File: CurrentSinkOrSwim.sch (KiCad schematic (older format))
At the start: 3 parts, among them P101 CONN_01X02, P102 CONN_01X03, P103 CONN_01X02

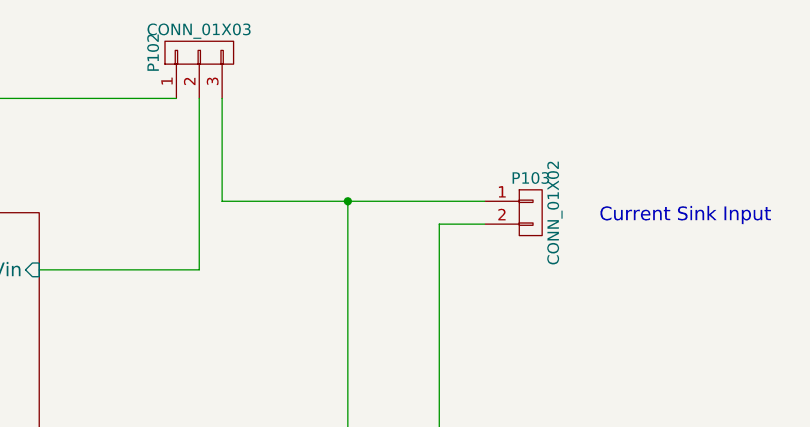
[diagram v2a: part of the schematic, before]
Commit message: added test points to  schematic and pcb
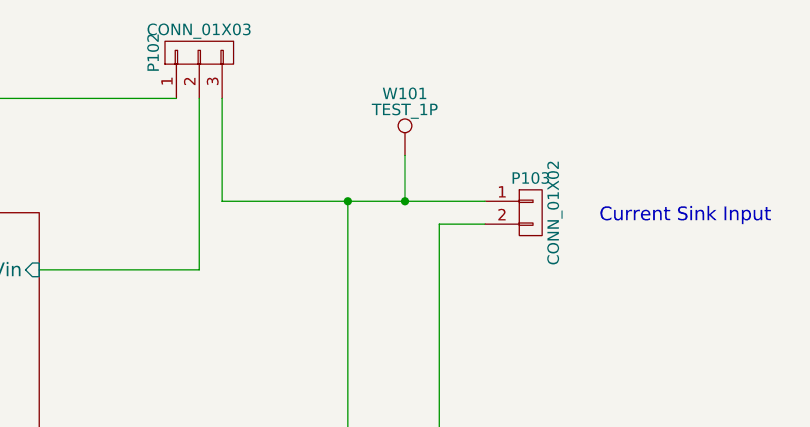
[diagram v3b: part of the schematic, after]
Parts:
- added W101: TEST_1P, Measurement_Points:Measurement_Point_Round-SMD-Pad_Small, symbol TEST_1P
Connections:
- net Current Control/Current_Sink+: now also W101.1
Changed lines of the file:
@@
 	6500 6000 7900 6000
 Connection ~ 7900 6000
+$Comp
+L TEST_1P W101
+U 1 1 57C85CB2
+P 7750 1050
+F 0 "W101" H 7750 1320 50  0000 C CNN
+F 1 "TEST_1P" H 7750 1250 50  0000 C CNN
+F 2 "Measurement_Points:Measurement_Point_Round-SMD-Pad_Small" H 7950 1050 50  0001 C CNN
+F 3 "" H 7950 1050 50  0000 C CNN
+	1    7750 1050
+	1    0    0    -1
+$EndComp
+Wire Wire Line
+	7750 1050 7750 1250
+Connection ~ 7750 1250
 $EndSCHEMATC

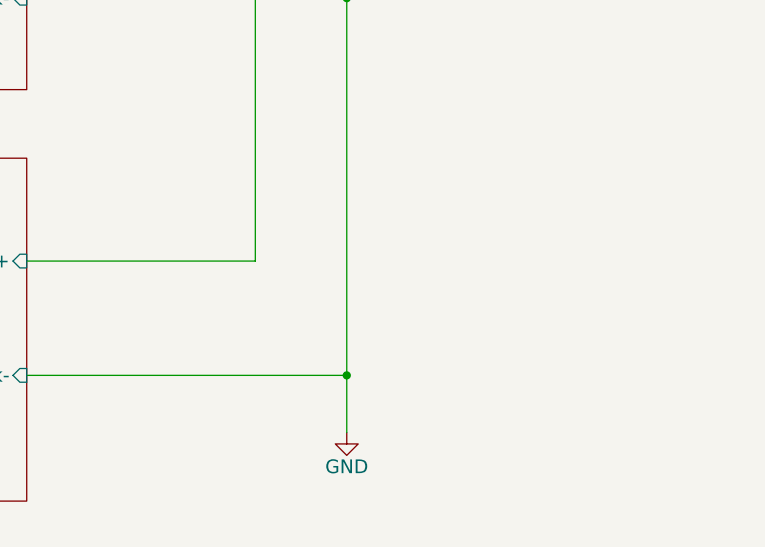
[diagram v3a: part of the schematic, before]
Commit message: added test point for GND
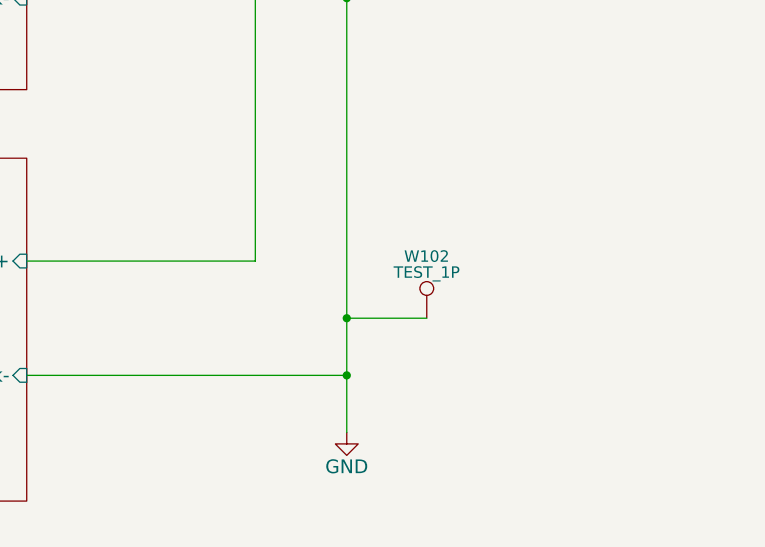
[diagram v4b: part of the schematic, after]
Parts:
- added W102: TEST_1P, Measurement_Points:Measurement_Point_Round-SMD-Pad_Small, symbol TEST_1P
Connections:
- net GND: now also W102.1
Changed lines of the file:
@@
 $EndComp
 $Comp
-L GND #PWR01
+L GND #PWR101
 U 1 1 54D85A15
 P 3350 1450
-F 0 "#PWR01" H 3350 1200 60  0001 C CNN
+F 0 "#PWR101" H 3350 1200 60  0001 C CNN
 F 1 "GND" H 3350 1300 60  0000 C CNN
 F 2 "" H 3350 1450 60  0000 C CNN
@@
 	4550 4400 4800 4400
 $Comp
-L GND #PWR02
+L GND #PWR102
 U 1 1 54DB4AD2
 P 7900 6250
-F 0 "#PWR02" H 7900 6000 60  0001 C CNN
+F 0 "#PWR102" H 7900 6000 60  0001 C CNN
 F 1 "GND" H 7900 6100 60  0000 C CNN
 F 2 "" H 7900 6250 60  0000 C CNN
@@
 	7750 1050 7750 1250
 Connection ~ 7750 1250
+$Comp
+L TEST_1P W102
+U 1 1 57C8C794
+P 8250 5750
+F 0 "W102" H 8250 6020 50  0000 C CNN
+F 1 "TEST_1P" H 8250 5950 50  0000 C CNN
+F 2 "Measurement_Points:Measurement_Point_Round-SMD-Pad_Small" H 8450 5750 50  0001 C CNN
+F 3 "" H 8450 5750 50  0000 C CNN
+	1    8250 5750
+	1    0    0    -1
+$EndComp
+Wire Wire Line
+	8250 5750 7900 5750
+Connection ~ 7900 5750
 $EndSCHEMATC
